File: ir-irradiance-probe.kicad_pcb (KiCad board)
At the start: 2 copper layers, 40 x 40 mm, 62 parts, among them J1 USB-C_UJC-HP-3-SMT-TR, J2 SM04B-SRSS-TB-LF-SN, J3 PinHeader_1x2_P2.54mm_Drill1.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, J4 Conn_BNC_031-70526-21, SW1 MSS3-V-T_R, U1 TLV70033_SC70, U2 AD8604ARUZ, U3 ADC101C027CIMK

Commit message: [#47284] Run kmake loclib
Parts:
- C12, C14, C2, C8: footprint antmicro-footprints:C_0402_1005Metric -> ir-irradiance-probe-footprints:C_0402_1005Metric
- C13, C4: footprint antmicro-footprints:C_0603_1608Metric -> ir-irradiance-probe-footprints:C_0603_1608Metric
- D9: footprint antmicro-footprints:Photodiode_SMD_4.2x5mm_TEMD -> ir-irradiance-probe-footprints:Photodiode_SMD_4.2x5mm_TEMD
- L1: footprint antmicro-footprints:L_0805_2012Metric -> ir-irradiance-probe-footprints:L_0805_2012Metric
- R4: footprint antmicro-footprints:R_0402_1005Metric -> ir-irradiance-probe-footprints:R_0402_1005Metric
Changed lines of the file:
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@@
     )
   )
-  (footprint "antmicro-footprints:C_0402_1005Metric" (layer "F.Cu")
+  (footprint "ir-irradiance-probe-footprints:C_0402_1005Metric" (layer "F.Cu")
     (at 74.28 100.81)
     (descr "Capacitor SMD 0402")
@@
     (pad "2" smd roundrect (at 0.484 0) (size 0.59 0.64) (layers "F.Cu" "F.Paste" "F.Mask") (roundrect_rratio 0.25)
       (net 12 "/5V_PWR_SUPPLY") (pintype "passive"))
-    (model "${ANT3DMDL}/C_0402_1005Metric.step"
+    (model "${KIPRJMOD}/lib/3d-models/C_0402_1005Metric.step"
       (offset (xyz 0 0 0.2))
       (scale (xyz 1 1 1))
@@
     )
   )
-  (footprint "antmicro-footprints:C_0402_1005Metric" (layer "F.Cu")
+  (footprint "ir-irradiance-probe-footprints:C_0402_1005Metric" (layer "F.Cu")
     (at 79.22 77.38 180)
     (descr "Capacitor SMD 0402")
@@
     (pad "2" smd roundrect (at 0.484 0 180) (size 0.59 0.64) (layers "F.Cu" "F.Paste" "F.Mask") (roundrect_rratio 0.25)
       (net 13 "/3V3_JST") (pintype "passive"))
-    (model "${ANT3DMDL}/C_0402_1005Metric.step"
+    (model "${KIPRJMOD}/lib/3d-models/C_0402_1005Metric.step"
       (offset (xyz 0 0 0.2))
       (scale (xyz 1 1 1))
@@
     )
   )
-  (footprint "antmicro-footprints:L_0805_2012Metric" (layer "F.Cu")
+  (footprint "ir-irradiance-probe-footprints:L_0805_2012Metric" (layer "F.Cu")
     (at 81.23 98.75)
     (descr "Inductor  SMD 0805")
@@
     (pad "2" smd rect (at 1.05 0) (size 1.2 1.2) (layers "F.Cu" "F.Paste" "F.Mask")
       (net 2 "/5V_FILTERED") (pintype "passive"))
-    (model "${ANT3DMDL}/L_0805_2012Metric.step"
+    (model "${KIPRJMOD}/lib/3d-models/L_0805_2012Metric.step"
       (offset (xyz 0 0 0))
       (scale (xyz 1 1 1))
@@
     (pad "1" thru_hole circle (at 0 0) (size 6.2 6.2) (drill 2.75) (layers *.Cu *.Mask))
   )
-  (footprint "antmicro-footprints:C_0402_1005Metric" (layer "F.Cu")
+  (footprint "ir-irradiance-probe-footprints:C_0402_1005Metric" (layer "F.Cu")
     (at 82.28 82.59 90)
     (descr "Capacitor SMD 0402")
@@
     (pad "2" smd roundrect (at 0.484 0 90) (size 0.59 0.64) (layers "F.Cu" "F.Paste" "F.Mask") (roundrect_rratio 0.25)
       (net 6 "Net-(U3-Pad3)") (pintype "passive"))
-    (model "${ANT3DMDL}/C_0402_1005Metric.step"
+    (model "${KIPRJMOD}/lib/3d-models/C_0402_1005Metric.step"
       (offset (xyz 0 0 0.2))
       (scale (xyz 1 1 1))
@@
     (pad "1" thru_hole circle (at 0 0) (size 6.2 6.2) (drill 2.75) (layers *.Cu *.Mask))
   )
-  (footprint "antmicro-footprints:R_0402_1005Metric" (layer "F.Cu")
+  (footprint "ir-irradiance-probe-footprints:R_0402_1005Metric" (layer "F.Cu")
     (at 83.28 82.59 -90)
     (descr "Resistor SMD 0402")
@@
     (pad "2" smd roundrect (at 0.485 0 270) (size 0.59 0.64) (layers "F.Cu" "F.Paste" "F.Mask") (roundrect_rratio 0.25)
       (net 22 "/ADC_IR_SIG_IN") (pintype "passive"))
-    (model "${ANT3DMDL}/R_0402_1005Metric.step"
+    (model "${KIPRJMOD}/lib/3d-models/R_0402_1005Metric.step"
       (offset (xyz 0 0 -0.01))
       (scale (xyz 1 1 1))
@@
     )
   )
-  (footprint "antmicro-footprints:C_0402_1005Metric" (layer "F.Cu")
+  (footprint "ir-irradiance-probe-footprints:C_0402_1005Metric" (layer "F.Cu")
     (at 78.79 97 180)
     (descr "Capacitor SMD 0402")
@@
     (pad "2" smd roundrect (at 0.484 0 180) (size 0.59 0.64) (layers "F.Cu" "F.Paste" "F.Mask") (roundrect_rratio 0.25)
       (net 11 "/5V_USB") (pintype "passive"))
-    (model "${ANT3DMDL}/C_0402_1005Metric.step"
+    (model "${KIPRJMOD}/lib/3d-models/C_0402_1005Metric.step"
       (offset (xyz 0 0 0.2))
       (scale (xyz 1 1 1))
@@
     )
   )
-  (footprint "antmicro-footprints:C_0603_1608Metric" (layer "F.Cu")
+  (footprint "ir-irradiance-probe-footprints:C_0603_1608Metric" (layer "F.Cu")
     (at 82.98 100.49 180)
     (descr "Capacitor SMD 0603")
@@
     (pad "2" smd roundrect (at 0.7 0 180) (size 0.6 0.8) (layers "F.Cu" "F.Paste" "F.Mask") (roundrect_rratio 0.2)
       (net 2 "/5V_FILTERED") (pintype "passive"))
-    (model "${ANT3DMDL}/C_0603_1608Metric.step"
+    (model "${KIPRJMOD}/lib/3d-models/C_0603_1608Metric.step"
       (offset (xyz 0 -0.45 0.42))
       (scale (xyz 1 1 1))
@@
     )
   )
-  (footprint "antmicro-footprints:C_0603_1608Metric" (layer "F.Cu")
+  (footprint "ir-irradiance-probe-footprints:C_0603_1608Metric" (layer "F.Cu")
     (at 77.87 99.36)
     (descr "Capacitor SMD 0603")
@@
     (pad "2" smd roundrect (at 0.7 0) (size 0.6 0.8) (layers "F.Cu" "F.Paste" "F.Mask") (roundrect_rratio 0.2)
       (net 3 "Net-(D1-Pad1)") (pintype "passive"))
-    (model "${ANT3DMDL}/C_0603_1608Metric.step"
+    (model "${KIPRJMOD}/lib/3d-models/C_0603_1608Metric.step"
       (offset (xyz 0 -0.45 0.42))
       (scale (xyz 1 1 1))
@@
       ) (layer "B.SilkS") (width 0) (fill solid))
   )
-  (footprint "antmicro-footprints:Photodiode_SMD_4.2x5mm_TEMD" (layer "B.Cu")
+  (footprint "ir-irradiance-probe-footprints:Photodiode_SMD_4.2x5mm_TEMD" (layer "B.Cu")
     (at 90 90 180)
     (property "Author" "Antmicro")
@@
       )
     )
-    (model "${ANT3DMDL}/Photodiode_SMD_4.2x5mm_TEMD.step"
+    (model "${KIPRJMOD}/lib/3d-models/Photodiode_SMD_4.2x5mm_TEMD.step"
       (offset (xyz 0 0 0))
       (scale (xyz 1 1 1))

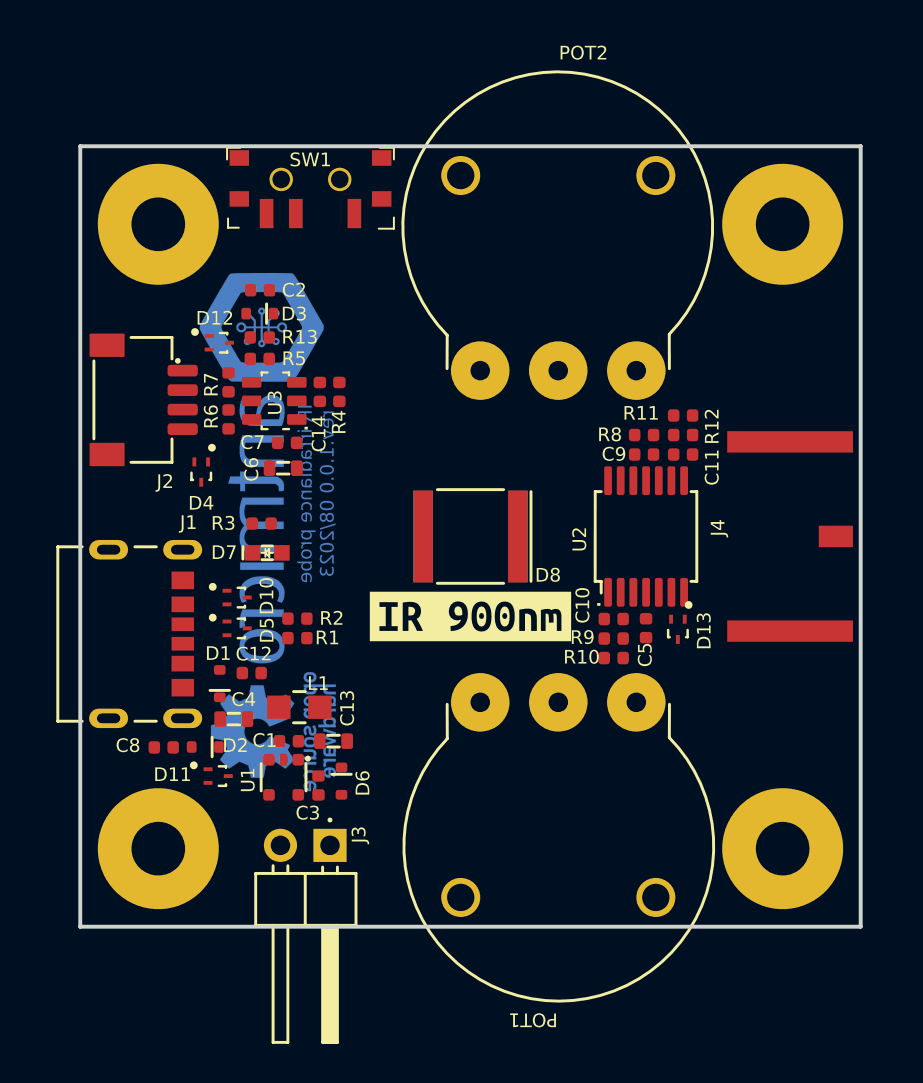
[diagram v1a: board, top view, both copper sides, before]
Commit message: [#47284] Standardized the rest of the components
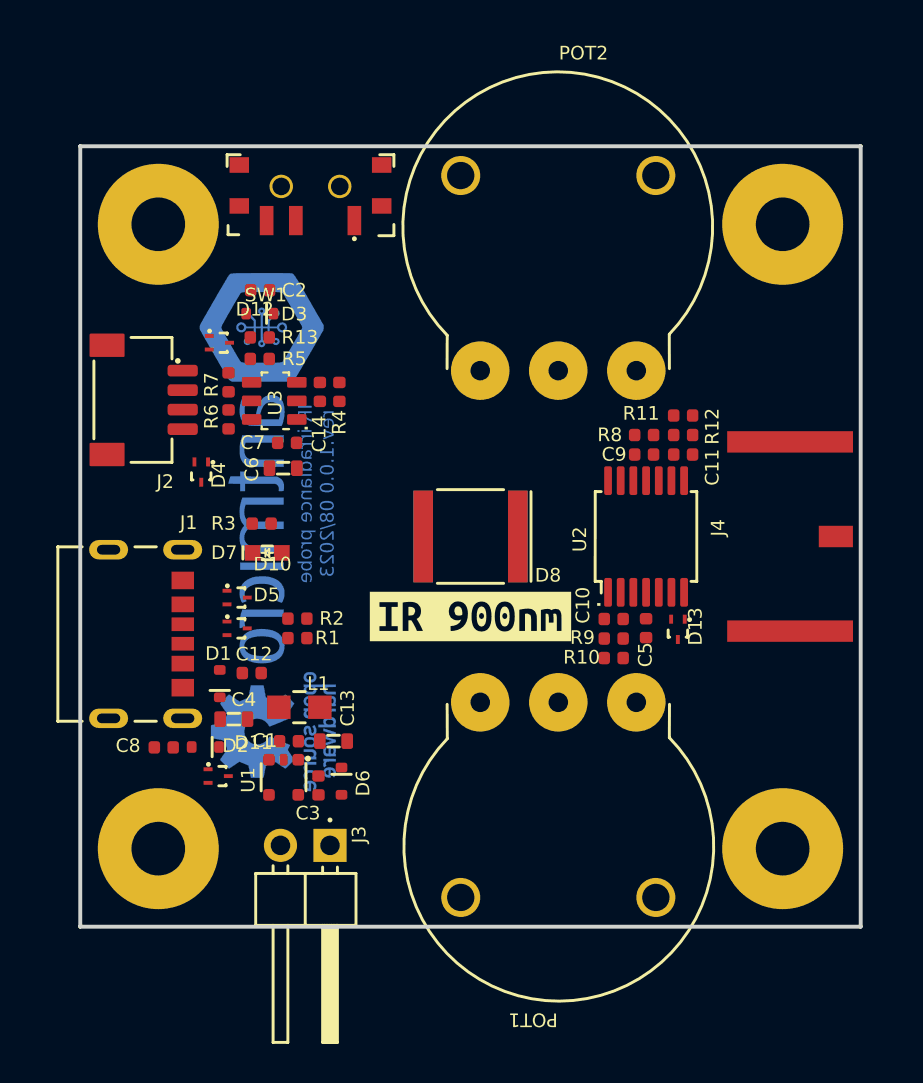
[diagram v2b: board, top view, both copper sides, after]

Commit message: [47284] Set stackup and constraints
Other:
- copper layers 2 -> 4
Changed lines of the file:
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@@
 (kicad_pcb (version 20211014) (generator pcbnew)
   (general
-    (thickness 1.6)
+    (thickness 1.576)
   )
   (paper "A4")
   (layers
     (0 "F.Cu" signal)
+    (1 "In1.Cu" signal)
+    (2 "In2.Cu" signal)
     (31 "B.Cu" signal)
     (32 "B.Adhes" user "B.Adhesive")
@@
   )
   (setup
+    (stackup
+      (layer "F.SilkS" (type "Top Silk Screen"))
+      (layer "F.Paste" (type "Top Solder Paste"))
+      (layer "F.Mask" (type "Top Solder Mask") (thickness 0.02))
+      (layer "F.Cu" (type "copper") (thickness 0.018))
+      (layer "dielectric 1" (type "prepreg") (thickness 0.36) (material "IS400 PR2116") (epsilon_r 4.06) (loss_tangent 0.0189))
+      (layer "In1.Cu" (type "copper") (thickness 0.035))
+      (layer "dielectric 2" (type "core") (thickness 0.71) (material "FR-4") (epsilon_r 4.35) (loss_tangent 0.02))
+      (layer "In2.Cu" (type "copper") (thickness 0.035))
+      (layer "dielectric 3" (type "prepreg") (thickness 0.36) (material "IS400 PR2116") (epsilon_r 4.06) (loss_tangent 0.0189))
+      (layer "B.Cu" (type "copper") (thickness 0.018))
+      (layer "B.Mask" (type "Bottom Solder Mask") (thickness 0.02))
+      (layer "B.Paste" (type "Bottom Solder Paste"))
+      (layer "B.SilkS" (type "Bottom Silk Screen"))
+      (copper_finish "None")
+      (dielectric_constraints no)
+    )
     (pad_to_mask_clearance 0)
     (pcbplotparams
@@
       (net 1 "GND") (pinfunction "GND") (pintype "passive"))
     (model "${KIPRJMOD}/lib/3d-models/TPD2E009DRTR.step"
-      (offset (xyz -0 -0 0))
+      (offset (xyz 0 0 0))
       (scale (xyz 1 1 1))
       (rotate (xyz -90 0 0))
@@
       (net 1 "GND") (pinfunction "GND") (pintype "passive"))
     (model "${KIPRJMOD}/lib/3d-models/TPD2E009DRTR.step"
-      (offset (xyz -0 -0 0))
+      (offset (xyz 0 0 0))
       (scale (xyz 1 1 1))
       (rotate (xyz -90 0 0))
@@
       (net 1 "GND") (pinfunction "GND") (pintype "passive"))
     (model "${KIPRJMOD}/lib/3d-models/TPD2E009DRTR.step"
-      (offset (xyz -0 -0 0))
+      (offset (xyz 0 0 0))
       (scale (xyz 1 1 1))
       (rotate (xyz -90 0 0))
@@
       (net 1 "GND") (pinfunction "GND") (pintype "passive"))
     (model "${KIPRJMOD}/lib/3d-models/TPD2E009DRTR.step"
-      (offset (xyz -0 -0 0))
+      (offset (xyz 0 0 0))
       (scale (xyz 1 1 1))
       (rotate (xyz -90 0 0))
@@
       (net 1 "GND") (pinfunction "GND") (pintype "passive"))
     (model "${KIPRJMOD}/lib/3d-models/TPD2E009DRTR.step"
-      (offset (xyz -0 -0 0))
+      (offset (xyz 0 0 0))
       (scale (xyz 1 1 1))
       (rotate (xyz -90 0 0))
@@
       (net 1 "GND") (pinfunction "GND") (pintype "passive"))
     (model "${KIPRJMOD}/lib/3d-models/TPD2E009DRTR.step"
-      (offset (xyz -0 -0 0))
+      (offset (xyz 0 0 0))
       (scale (xyz 1 1 1))
       (rotate (xyz -90 0 0))
@@
     (effects (font (size 0.7 0.7) (thickness 0.15)) (justify mirror))
   )
+  (segment (start 77.583 83.498) (end 77.6 83.515) (width 0.2) (layer "F.Cu") (net 14))
   (group "" (id 4a432a2e-19b5-4648-a079-f9ebe9626ea7)
     (members

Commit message: [47284] Add preliminary routing
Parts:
- removed kibuzzard-64C24DFB: G***, kibuzzard-64C24DFB
- removed kibuzzard-64C24E0E: G***, kibuzzard-64C24E0E
- removed kibuzzard-64C24E25: G***, kibuzzard-64C24E25
- moved D13 3.22 mm to (102.8, 92.3), turned to 90 degrees
- moved D12 1.39 mm to (76.3, 78.9), turned to 180 degrees
- moved R13 1.21 mm to (78.3, 80.6), turned to 0 degrees
- moved C7 1.11 mm to (81.6, 85.7), turned to 180 degrees
- moved N1 1.09 mm to (79.5, 87.6)
- moved R6 1.09 mm to (77.6, 85.1)
- moved R7 1.09 mm to (77.6, 83.2)
- moved R10 1.00 mm to (97.3, 95.2)
- moved R9 1.00 mm to (97.3, 96.2)
- moved R8 0.97 mm to (97.9, 84.8), turned to 0 degrees
- moved R11 0.96 mm to (99.9, 83.8), turned to 180 degrees
- moved R5 0.68 mm to (79.2, 81.6)
- moved C5 0.68 mm to (99.5, 94.2), turned to 0 degrees
- moved U3 0.61 mm to (80.0, 83.7)
- moved C14 0.60 mm to (82.3, 83.2)
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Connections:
- SW1 pad 1: /IR_900nm_OP_AMP_OUT -> /IR_940nm_OP_AMP_OUT
- SW1 pad 3: /IR_940nm_OP_AMP_OUT -> /IR_900nm_OP_AMP_OUT
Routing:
- net +3.3VA: track 0.00 -> 75.0 mm, vias 0 -> 4
- net GND: track 0.00 -> 57.7 mm, vias 0 -> 127
- net /IR_900nm_OP_AMP_OUT: track 0.00 -> 41.5 mm
- net /SELECTED_IR_SIG: track 0.00 -> 34.5 mm
- net /IR_940nm_OP_AMP_OUT: track 0.00 -> 27.7 mm
- net Net-(C11-Pad1): track 0.00 -> 22.3 mm, vias 0 -> 1
- net /ADC_IR_SIG_IN: track 0.00 -> 15.9 mm, vias 0 -> 2
- net Net-(C10-Pad1): track 0.00 -> 11.0 mm
- net /5V_USB: track 0.00 -> 10.3 mm
- net Net-(POT2-Pad1): track 0.00 -> 9.91 mm
- net Net-(D13-Pad1): track 0.00 -> 9.61 mm
- net /5V_PWR_SUPPLY: track 0.00 -> 8.34 mm
- net /3V3_JST: track 0.00 -> 7.54 mm
- net Net-(C4-Pad2): track 0.00 -> 6.23 mm
- net /SDA: track 0.02 -> 6.15 mm
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- added copper zone on F.Cu, net /5V_USB
- added copper zone on F.Cu, net GND
- added copper zone on In1.Cu, net GND
- added copper zone on In2.Cu, net GND

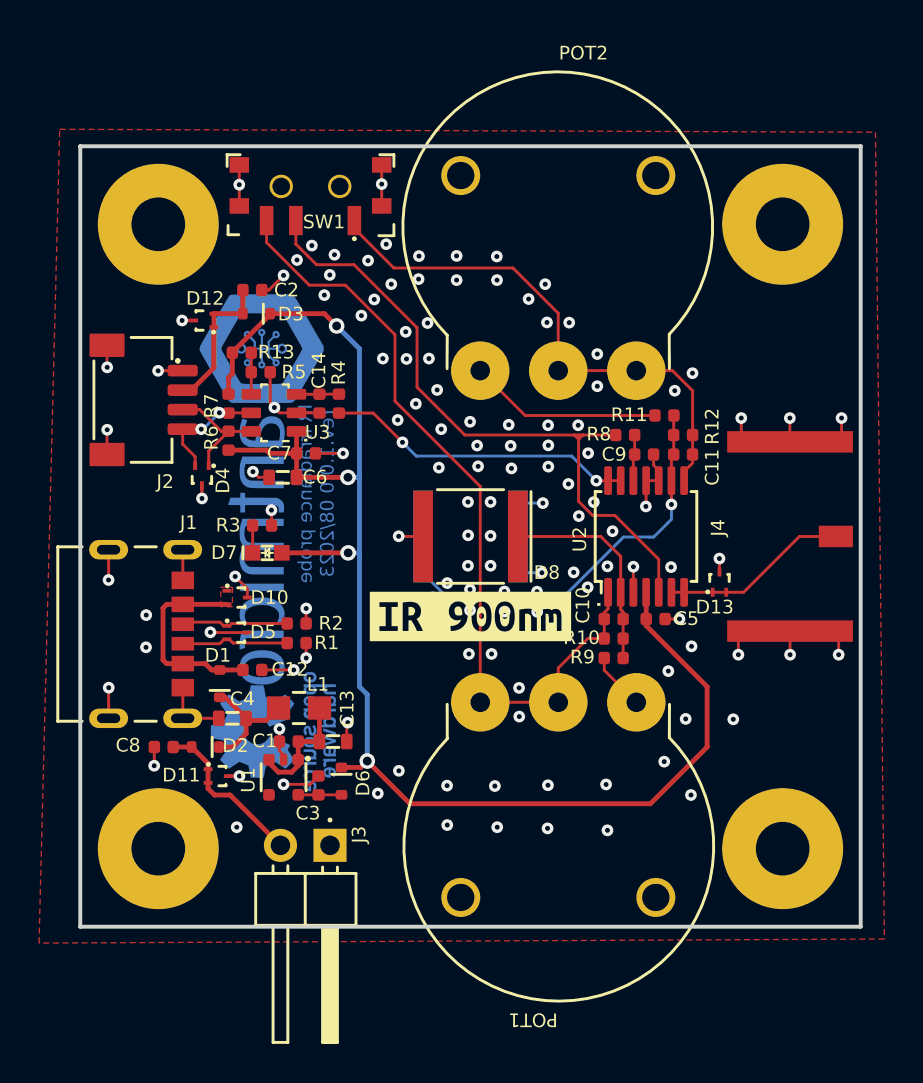
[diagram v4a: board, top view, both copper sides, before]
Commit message: [47284] Clear DRC errors and warnings
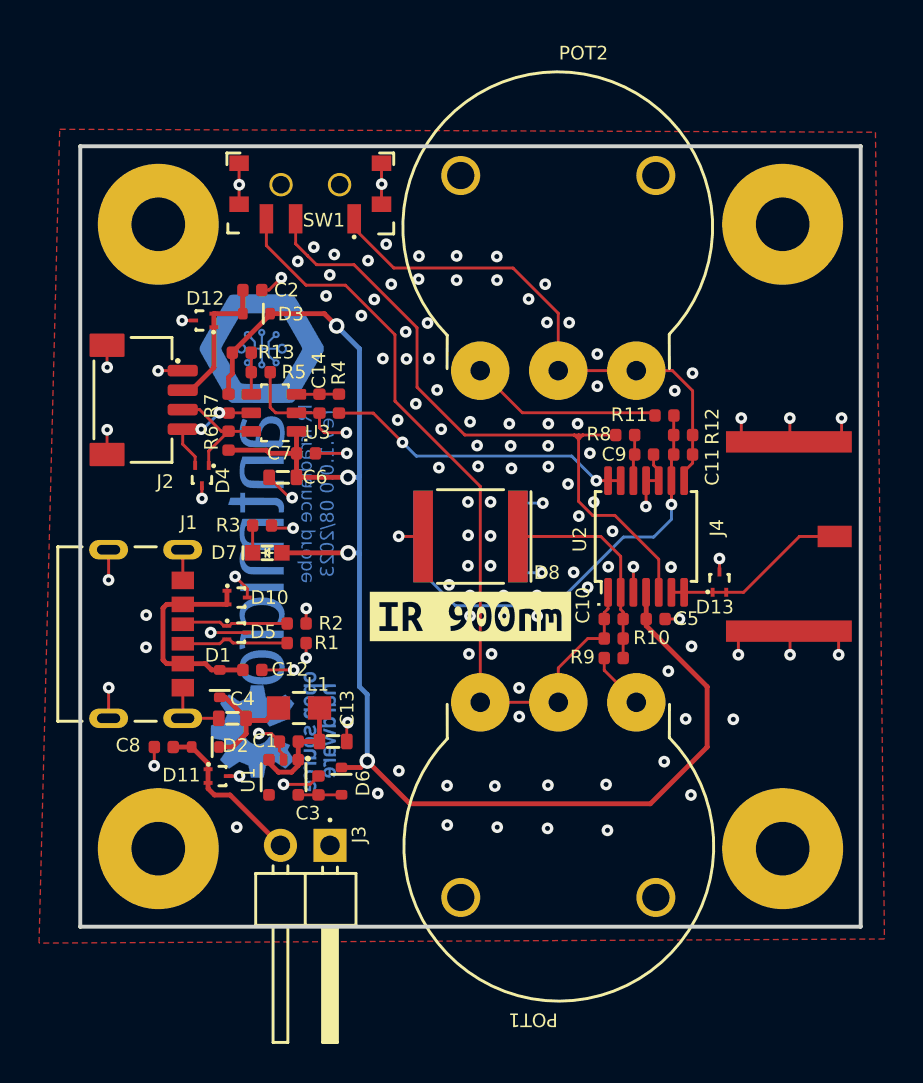
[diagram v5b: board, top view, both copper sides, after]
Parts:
- moved SW1 0.09 mm to (81.8, 71.6)
- moved J4 0.06 mm to (116.5, 90.0)
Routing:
- net GND: track 57.7 -> 61.3 mm
- net /5V_USB: track 10.3 -> 11.0 mm
- removed copper zone on F.Cu, net /5V_USB
